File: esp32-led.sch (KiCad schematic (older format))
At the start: 10 parts, among them J1 LED Connector, J2 USB4125-GF-A_REVA2, J3 LED Connector, U1 SN74AHCT125D, U2 ESP32_NODEMCU

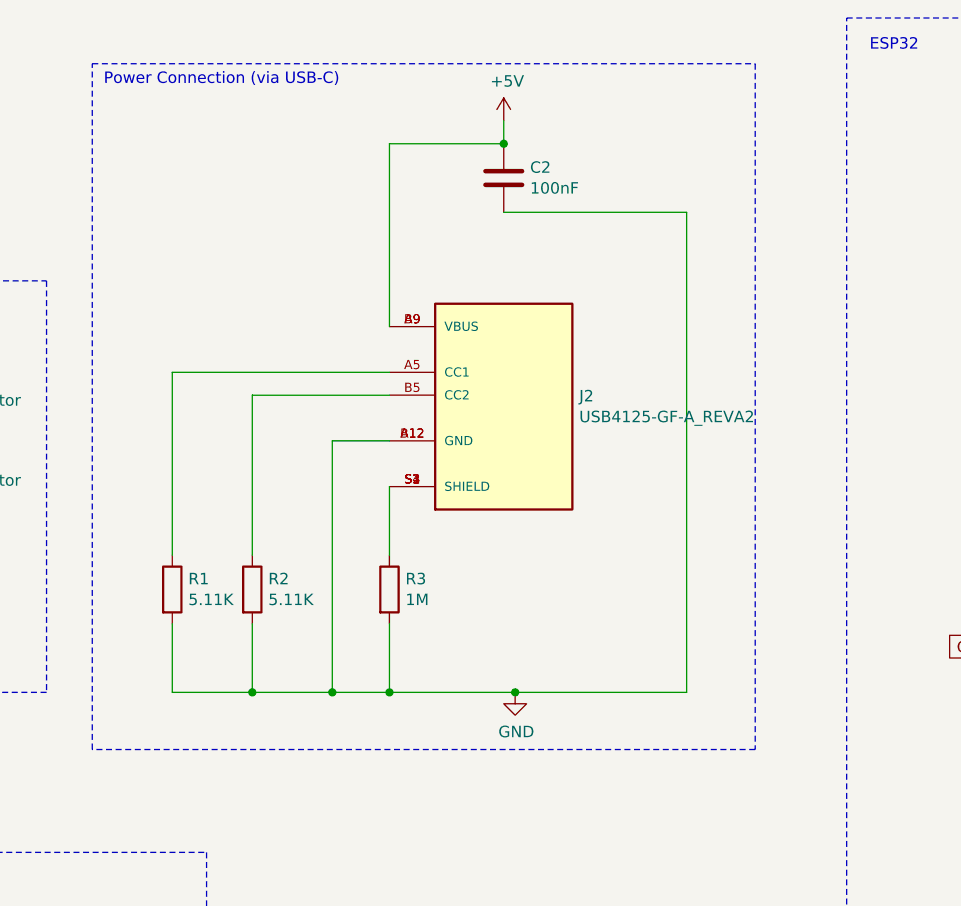
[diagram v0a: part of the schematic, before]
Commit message: Added barrel jack version
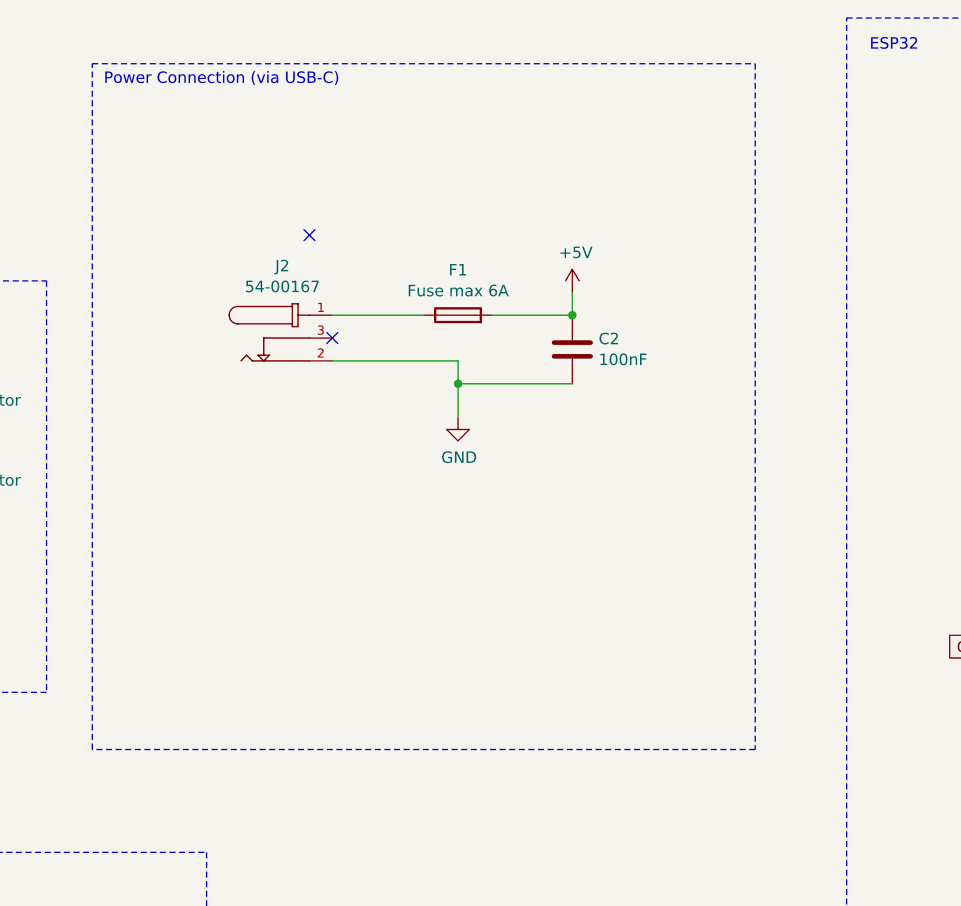
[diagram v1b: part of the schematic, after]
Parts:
- removed J2: USB4125-GF-A_REVA2, USB4125-GF-A_REVA2:GCT_USB4125-GF-A_REVA2, symbol USB4125-GF-A_REVA2:USB4125-GF-A_REVA2
- removed R1, R2: 5.11K, Resistor_SMD:R_0805_2012Metric_Pad1.20x1.40mm_HandSolder, symbol Device:R
- removed R3: 1M, Resistor_SMD:R_0805_2012Metric_Pad1.20x1.40mm_HandSolder, symbol Device:R
- added F1: Fuse max 6A, Fuse:Fuse_1206_3216Metric_Pad1.42x1.75mm_HandSolder, symbol Device:Fuse
- added J2: 54-00167, 54-00167:TENSILITY_54-00167, symbol 54-00167:54-00167
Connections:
- net +5V: now also F1.2
- net GND: now also J2.2
- new net: F1.1, J2.1
- no-connect marks 39 -> 41
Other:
- moved on the sheet: C2
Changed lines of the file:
@@
 $EndDescr
-$Comp
-L USB4125-GF-A_REVA2:USB4125-GF-A_REVA2 J2
-U 1 1 62E70613
-P 5450 2300
-F 0 "J2" H 5780 2296 50  0000 L CNN
-F 1 "USB4125-GF-A_REVA2" H 5780 2205 50  0000 L CNN
-F 2 "USB4125-GF-A_REVA2:GCT_USB4125-GF-A_REVA2" H 5450 2300 50  0001 L BNN
-F 3 "" H 5450 2300 50  0001 L BNN
-F 4 "GCT" H 5450 2300 50  0001 L BNN "MANUFACTURER"
-F 5 "Rev A2" H 5450 2300 50  0001 L BNN "PARTREV"
-F 6 "3.16 mm" H 5450 2300 50  0001 L BNN "MAXIMUM_PACKAGE_HEIGHT"
-F 7 "Manufacturer Recommendations" H 5450 2300 50  0001 L BNN "STANDARD"
-	1    5450 2300
-	1    0    0    -1
-$EndComp
 $Comp
 L power:+5V #PWR05
 U 1 1 62E71C0E
-P 5450 1100
-F 0 "#PWR05" H 5450 950 50  0001 C CNN
-F 1 "+5V" H 5465 1273 50  0000 C CNN
-F 2 "" H 5450 1100 50  0001 C CNN
-F 3 "" H 5450 1100 50  0001 C CNN
-	1    5450 1100
+P 5750 1850
+F 0 "#PWR05" H 5750 1700 50  0001 C CNN
+F 1 "+5V" H 5765 2023 50  0000 C CNN
+F 2 "" H 5750 1850 50  0001 C CNN
+F 3 "" H 5750 1850 50  0001 C CNN
+	1    5750 1850
 	1    0    0    -1
 $EndComp
@@
 L power:GND #PWR06
 U 1 1 62E7243B
-P 5500 3600
-F 0 "#PWR06" H 5500 3350 50  0001 C CNN
-F 1 "GND" H 5505 3427 50  0000 C CNN
-F 2 "" H 5500 3600 50  0001 C CNN
-F 3 "" H 5500 3600 50  0001 C CNN
-	1    5500 3600
-	1    0    0    -1
-$EndComp
-$Comp
-L Device:R R3
-U 1 1 62E72F7A
-P 4950 3150
-F 0 "R3" H 5020 3196 50  0000 L CNN
-F 1 "1M" H 5020 3105 50  0000 L CNN
-F 2 "Resistor_SMD:R_0805_2012Metric_Pad1.20x1.40mm_HandSolder" V 4880 3150 50  0001 C CNN
-F 3 "~" H 4950 3150 50  0001 C CNN
-	1    4950 3150
-	1    0    0    -1
-$EndComp
-$Comp
-L Device:R R2
-U 1 1 62E74433
-P 4350 3150
-F 0 "R2" H 4420 3196 50  0000 L CNN
-F 1 "5.11K" H 4420 3105 50  0000 L CNN
-F 2 "Resistor_SMD:R_0805_2012Metric_Pad1.20x1.40mm_HandSolder" V 4280 3150 50  0001 C CNN
-F 3 "~" H 4350 3150 50  0001 C CNN
-	1    4350 3150
-	1    0    0    -1
-$EndComp
-$Comp
-L Device:R R1
-U 1 1 62E758CD
-P 4000 3150
-F 0 "R1" H 4070 3196 50  0000 L CNN
-F 1 "5.11K" H 4070 3105 50  0000 L CNN
-F 2 "Resistor_SMD:R_0805_2012Metric_Pad1.20x1.40mm_HandSolder" V 3930 3150 50  0001 C CNN
-F 3 "~" H 4000 3150 50  0001 C CNN
-	1    4000 3150
-	1    0    0    -1
-$EndComp
-Wire Wire Line
-	4950 2700 4950 3000
-Wire Wire Line
-	4950 3300 4950 3600
-Wire Wire Line
-	4950 3600 5500 3600
-Wire Wire Line
-	4950 2500 4700 2500
-Wire Wire Line
-	4700 2500 4700 3600
-Wire Wire Line
-	4700 3600 4950 3600
-Connection ~ 4950 3600
-Wire Wire Line
-	4950 2300 4350 2300
-Wire Wire Line
-	4350 2300 4350 3000
-Wire Wire Line
-	4950 2200 4000 2200
-Wire Wire Line
-	4000 2200 4000 3000
-Wire Wire Line
-	4350 3300 4350 3600
-Wire Wire Line
-	4350 3600 4700 3600
-Connection ~ 4700 3600
-Wire Wire Line
-	4000 3300 4000 3600
-Wire Wire Line
-	4000 3600 4350 3600
-Connection ~ 4350 3600
+P 5250 2400
+F 0 "#PWR06" H 5250 2150 50  0001 C CNN
+F 1 "GND" H 5255 2227 50  0000 C CNN
+F 2 "" H 5250 2400 50  0001 C CNN
+F 3 "" H 5250 2400 50  0001 C CNN
+	1    5250 2400
+	1    0    0    -1
+$EndComp
 $Comp
 L Device:C C2
 U 1 1 62E7BB21
-P 5450 1350
-F 0 "C2" H 5565 1396 50  0000 L CNN
-F 1 "100nF" H 5565 1305 50  0000 L CNN
-F 2 "Capacitor_SMD:C_0805_2012Metric_Pad1.18x1.45mm_HandSolder" H 5488 1200 50  0001 C CNN
-F 3 "~" H 5450 1350 50  0001 C CNN
-	1    5450 1350
-	1    0    0    -1
-$EndComp
-Wire Wire Line
-	4950 2000 4950 1200
-Wire Wire Line
-	4950 1200 5450 1200
-Wire Wire Line
-	5450 1100 5450 1200
-Connection ~ 5450 1200
-Wire Wire Line
-	5450 1500 6250 1500
-Wire Wire Line
-	6250 1500 6250 3600
-Wire Wire Line
-	6250 3600 5500 3600
-Connection ~ 5500 3600
+P 5750 2100
+F 0 "C2" H 5865 2146 50  0000 L CNN
+F 1 "100nF" H 5865 2055 50  0000 L CNN
+F 2 "Capacitor_SMD:C_0805_2012Metric_Pad1.18x1.45mm_HandSolder" H 5788 1950 50  0001 C CNN
+F 3 "~" H 5750 2100 50  0001 C CNN
+	1    5750 2100
+	1    0    0    -1
+$EndComp
+Wire Wire Line
+	5750 1850 5750 1950
 Wire Notes Line
 	6550 850  6550 3850
@@
 	2450 2750 1950 2750
 Connection ~ 2450 2750
+$Comp
+L Device:Fuse F1
+U 1 1 62EAB667
+P 5250 1950
+F 0 "F1" V 5447 1950 50  0000 C CNN
+F 1 "Fuse max 6A" V 5356 1950 50  0000 C CNN
+F 2 "Fuse:Fuse_1206_3216Metric_Pad1.42x1.75mm_HandSolder" V 5180 1950 50  0001 C CNN
+F 3 "~" H 5250 1950 50  0001 C CNN
+	1    5250 1950
+	0    -1   -1   0
+$EndComp
+Wire Wire Line
+	4700 2150 5250 2150
+Wire Wire Line
+	5250 2150 5250 2250
+Wire Wire Line
+	4700 1950 5100 1950
+Wire Wire Line
+	5400 1950 5750 1950
+Connection ~ 5750 1950
+Wire Wire Line
+	5750 2250 5250 2250
+Connection ~ 5250 2250
+Wire Wire Line
+	5250 2250 5250 2400
+NoConn ~ 4600 1600
+$Comp
+L 54-00167:54-00167 J2
+U 1 1 62EBE3AD
+P 4400 1950
+F 0 "J2" H 4482 2165 50  0000 C CNN
+F 1 "54-00167" H 4482 2074 50  0000 C CNN
+F 2 "54-00167:TENSILITY_54-00167" H 4400 1950 50  0001 L BNN
+F 3 "" H 4400 1950 50  0001 L BNN
+F 4 "11.3mm" H 4400 1950 50  0001 L BNN "MAXIMUM_PACKAGE_HEIGHT"
+F 5 "Tensility" H 4400 1950 50  0001 L BNN "MANUFACTURER"
+F 6 "A" H 4400 1950 50  0001 L BNN "PARTREV"
+F 7 "Manufacturer Recommendations" H 4400 1950 50  0001 L BNN "STANDARD"
+	1    4400 1950
+	1    0    0    -1
+$EndComp
+NoConn ~ 4700 2050
 $EndSCHEMATC

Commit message: Changed the wrong esp32 footprint
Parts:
- removed U2: ESP32_NODEMCU, ESP32_NODEMCU:MODULE_ESP32_NODEMCU, symbol ESP32_NODEMCU:ESP32_NODEMCU
- added U2: ESP32-DEVKITC-32D, ESP32-DEVKITC-32D:MODULE_ESP32-DEVKITC-32D, symbol ESP32-DEVKITC-32D:ESP32-DEVKITC-32D
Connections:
- net +5V: now also U2.19 (EXT_5V)
- net GND: now also U2.14 (GND1)
- net GPIO4: now also U2.34 (IO2)
- no-connect marks 41 -> 42
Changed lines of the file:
@@
 Wire Notes Line
 	10300 650  10300 5200
-Wire Wire Line
-	8400 3400 7700 3400
-Text GLabel 7700 3400 0    50   Input ~ 0
+Text GLabel 9800 2900 2    50   Input ~ 0
 GPIO4
-Wire Wire Line
-	10000 4650 9250 4650
-Wire Wire Line
-	10000 3900 10000 4650
 $Comp
 L power:GND #PWR08
 U 1 1 62EA1CA8
-P 9250 4650
-F 0 "#PWR08" H 9250 4400 50  0001 C CNN
-F 1 "GND" H 9255 4477 50  0000 C CNN
-F 2 "" H 9250 4650 50  0001 C CNN
-F 3 "" H 9250 4650 50  0001 C CNN
-	1    9250 4650
-	1    0    0    -1
-$EndComp
-NoConn ~ 10000 1700
-NoConn ~ 10000 1900
-NoConn ~ 10000 2000
-NoConn ~ 10000 2200
-NoConn ~ 10000 2300
-NoConn ~ 10000 2400
-NoConn ~ 10000 2500
-NoConn ~ 10000 2600
-NoConn ~ 10000 2700
-NoConn ~ 10000 2800
-NoConn ~ 10000 2900
-NoConn ~ 10000 3000
-NoConn ~ 10000 3100
-NoConn ~ 10000 3200
-NoConn ~ 10000 3300
-NoConn ~ 10000 3400
-NoConn ~ 10000 3500
-NoConn ~ 10000 3600
-NoConn ~ 10000 3700
-NoConn ~ 8400 3700
-NoConn ~ 8400 3600
-NoConn ~ 8400 3500
-NoConn ~ 8400 3300
-NoConn ~ 8400 3200
-NoConn ~ 8400 3000
-NoConn ~ 8400 2800
-NoConn ~ 8400 2700
-NoConn ~ 8400 2600
-NoConn ~ 8400 2500
-NoConn ~ 8400 2300
-NoConn ~ 8400 2100
-NoConn ~ 8400 2000
-NoConn ~ 8400 1900
-$Comp
-L ESP32_NODEMCU:ESP32_NODEMCU U2
-U 1 1 62E9349D
-P 9200 2700
-F 0 "U2" H 9200 4067 50  0000 C CNN
-F 1 "ESP32_NODEMCU" H 9200 3976 50  0000 C CNN
-F 2 "ESP32_NODEMCU:MODULE_ESP32_NODEMCU" H 9200 2700 50  0001 L BNN
-F 3 "" H 9200 2700 50  0001 L BNN
-F 4 "6.6 mm" H 9200 2700 50  0001 L BNN "MAXIMUM_PACKAGE_HEIGHT"
-F 5 "Espressif" H 9200 2700 50  0001 L BNN "MANUFACTURER"
-F 6 "Manufacturer Recommendations" H 9200 2700 50  0001 L BNN "STANDARD"
-	1    9200 2700
-	1    0    0    -1
-$EndComp
-Wire Wire Line
-	10000 950  10000 1600
-Wire Wire Line
-	9200 950  10000 950
+P 7150 2850
+F 0 "#PWR08" H 7150 2600 50  0001 C CNN
+F 1 "GND" H 7155 2677 50  0000 C CNN
+F 2 "" H 7150 2850 50  0001 C CNN
+F 3 "" H 7150 2850 50  0001 C CNN
+	1    7150 2850
+	1    0    0    -1
+$EndComp
+Wire Wire Line
+	7100 3300 7900 3300
 $Comp
 L power:+5V #PWR07
 U 1 1 62E9556F
-P 9200 950
-F 0 "#PWR07" H 9200 800 50  0001 C CNN
-F 1 "+5V" H 9215 1123 50  0000 C CNN
-F 2 "" H 9200 950 50  0001 C CNN
-F 3 "" H 9200 950 50  0001 C CNN
-	1    9200 950
+P 7100 3300
+F 0 "#PWR07" H 7100 3150 50  0001 C CNN
+F 1 "+5V" H 7115 3473 50  0000 C CNN
+F 2 "" H 7100 3300 50  0001 C CNN
+F 3 "" H 7100 3300 50  0001 C CNN
+	1    7100 3300
 	1    0    0    -1
 $EndComp
@@
 Wire Wire Line
 	5250 2250 5250 2400
-NoConn ~ 4600 1600
 $Comp
 L 54-00167:54-00167 J2
@@
 $EndComp
 NoConn ~ 4700 2050
+$Comp
+L ESP32-DEVKITC-32D:ESP32-DEVKITC-32D U2
+U 1 1 6300BAA5
+P 8700 2400
+F 0 "U2" H 8700 3567 50  0000 C CNN
+F 1 "ESP32-DEVKITC-32D" H 8700 3476 50  0000 C CNN
+F 2 "ESP32-DEVKITC-32D:MODULE_ESP32-DEVKITC-32D" H 8700 2400 50  0001 L BNN
+F 3 "" H 8700 2400 50  0001 L BNN
+F 4 "Espressif Systems" H 8700 2400 50  0001 L BNN "MANUFACTURER"
+F 5 "4" H 8700 2400 50  0001 L BNN "PARTREV"
+	1    8700 2400
+	1    0    0    -1
+$EndComp
+Wire Wire Line
+	7900 2800 7150 2800
+Wire Wire Line
+	7150 2800 7150 2850
+Wire Wire Line
+	9500 2900 9800 2900
+NoConn ~ 9500 1500
+NoConn ~ 9500 1600
+NoConn ~ 9500 1700
+NoConn ~ 9500 1800
+NoConn ~ 9500 1900
+NoConn ~ 9500 2000
+NoConn ~ 9500 2100
+NoConn ~ 9500 2200
+NoConn ~ 9500 2300
+NoConn ~ 9500 2400
+NoConn ~ 9500 2500
+NoConn ~ 9500 2600
+NoConn ~ 9500 2700
+NoConn ~ 9500 2800
+NoConn ~ 9500 3000
+NoConn ~ 9500 3100
+NoConn ~ 9500 3200
+NoConn ~ 9500 3300
+NoConn ~ 7900 1500
+NoConn ~ 7900 1600
+NoConn ~ 7900 1700
+NoConn ~ 7900 1800
+NoConn ~ 7900 1900
+NoConn ~ 7900 2000
+NoConn ~ 7900 2100
+NoConn ~ 7900 2200
+NoConn ~ 7900 2300
+NoConn ~ 7900 2400
+NoConn ~ 7900 2500
+NoConn ~ 7900 2600
+NoConn ~ 7900 2700
+NoConn ~ 7900 2900
+NoConn ~ 7900 3000
+NoConn ~ 7900 3100
+NoConn ~ 7900 3200
 $EndSCHEMATC
